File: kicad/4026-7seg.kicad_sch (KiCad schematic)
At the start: 2 parts, among them U5 D168K, U6 4026

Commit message: Note BOM effects in different implementations
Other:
- note added: "KNOWN ISSUES: * no easy reset * starts at 0, not 1 BOM ADDITION: 2"
- note removed: "KNOWN ISSUES: * no easy reset * starts at 0, not 1"
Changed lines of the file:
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@@
     (stroke (width 0) (type default) (color 0 0 0 0))
   )
-  (text "KNOWN ISSUES:\n* no easy reset\n* starts at 0, not 1"
-    (at 154.305 121.285 0)
+  (text "KNOWN ISSUES:\n* no easy reset\n* starts at 0, not 1\n\nBOM ADDITION: 2"
+    (at 153.67 127.635 0)
     (effects (font (size 1.27 1.27)) (justify left bottom))
   )

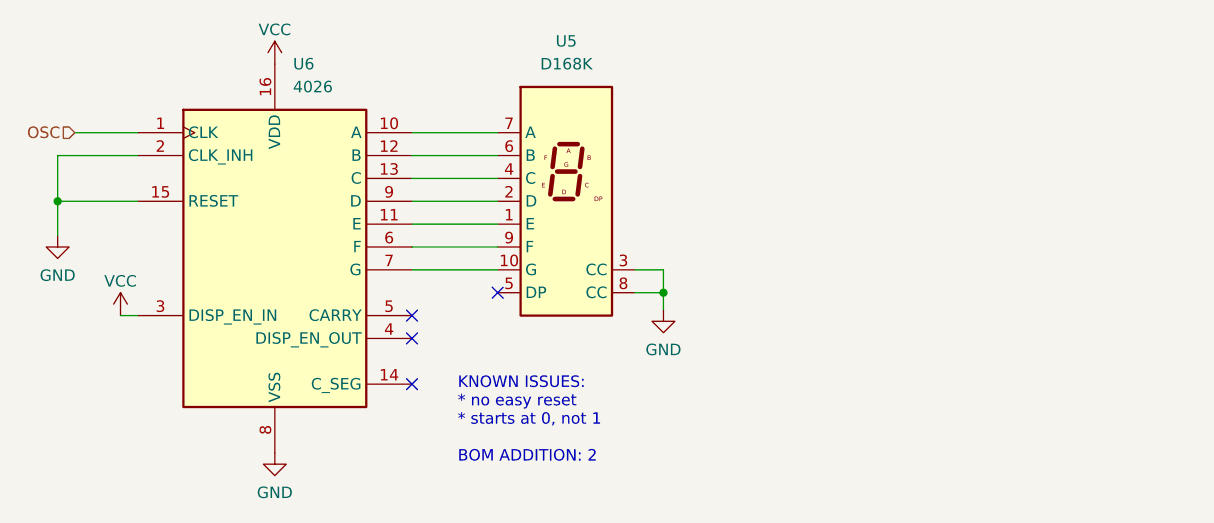
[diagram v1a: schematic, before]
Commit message: Hmmm, may need resistors for LED driver ICs
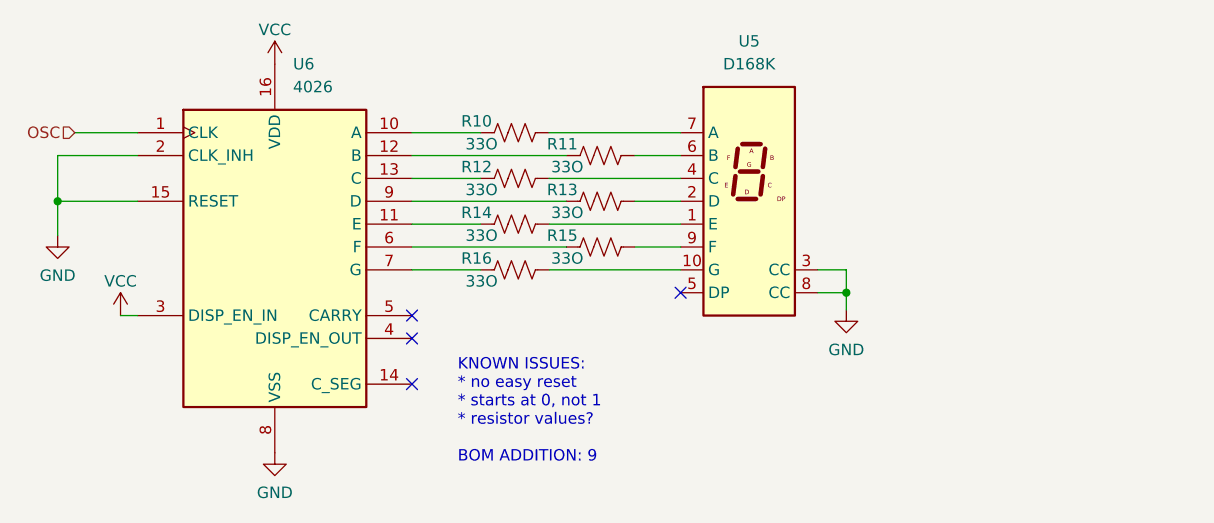
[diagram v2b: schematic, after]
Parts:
- added R10, R11, R12, R13, R14, R15, R16: 33O, Resistor_THT:R_Axial_DIN0204_L3.6mm_D1.6mm_P7.62mm_Horizontal, symbol Device:R_US
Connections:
- net at U5.1 (E): now also R14.2; no longer U6.11 (E)
- net at U5.10 (G): now also R16.2; no longer U6.7 (G)
- net at U5.2 (D): now also R13.2; no longer U6.9 (D)
- net at U6.13 (C): now also R12.1; no longer U5.4 (C)
- net at U5.6 (B): now also R11.2; no longer U6.12 (B)
- net at U5.7 (A): now also R10.2; no longer U6.10 (A)
- net at U6.6 (F): now also R15.1; no longer U5.9 (F)
- new net: R12.2, U5.4 (C)
- new net: R15.2, U5.9 (F)
- new net: R16.1, U6.7 (G)
- new net: R13.1, U6.9 (D)
- new net: R10.1, U6.10 (A)
- new net: R14.1, U6.11 (E)
- new net: R11.1, U6.12 (B)
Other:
- note added: "KNOWN ISSUES: * no easy reset * starts at 0, not 1 * resistor values? BOM ADDITION: 9"
- note removed: "KNOWN ISSUES: * no easy reset * starts at 0, not 1 BOM ADDITION: 2"
- moved on the sheet: U5

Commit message: TODO: fix 7seg footprint
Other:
- note added: "TODO: fix footprint! 10 A 9 B 7 C 5 D 4 E 2 F 1 G 6 DP 3 COM 8 COM"
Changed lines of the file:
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@@
+    (effects (font (size 1.27 1.27)) (justify left bottom))
+  )
+  (text "TODO: fix footprint!\n\n10 A\n9  B\n7  C\n5  D\n4  E\n2  F\n1  G\n\n6  DP\n3  COM\n8  COM"
+    (at 210.82 107.95 0)
     (effects (font (size 1.27 1.27)) (justify left bottom))
   )

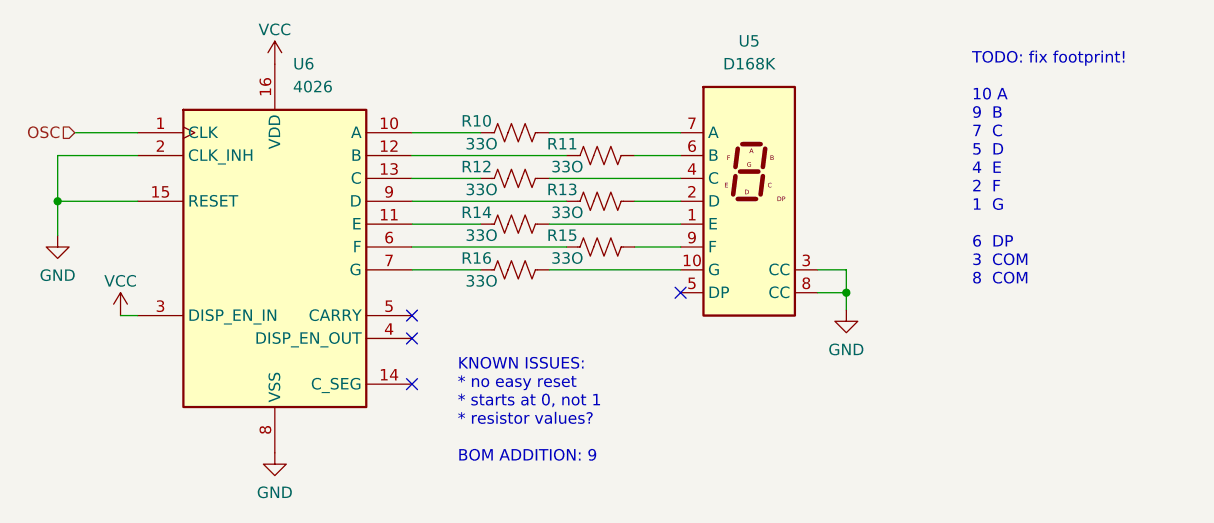
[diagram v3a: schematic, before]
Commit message: Fix 7seg footprint
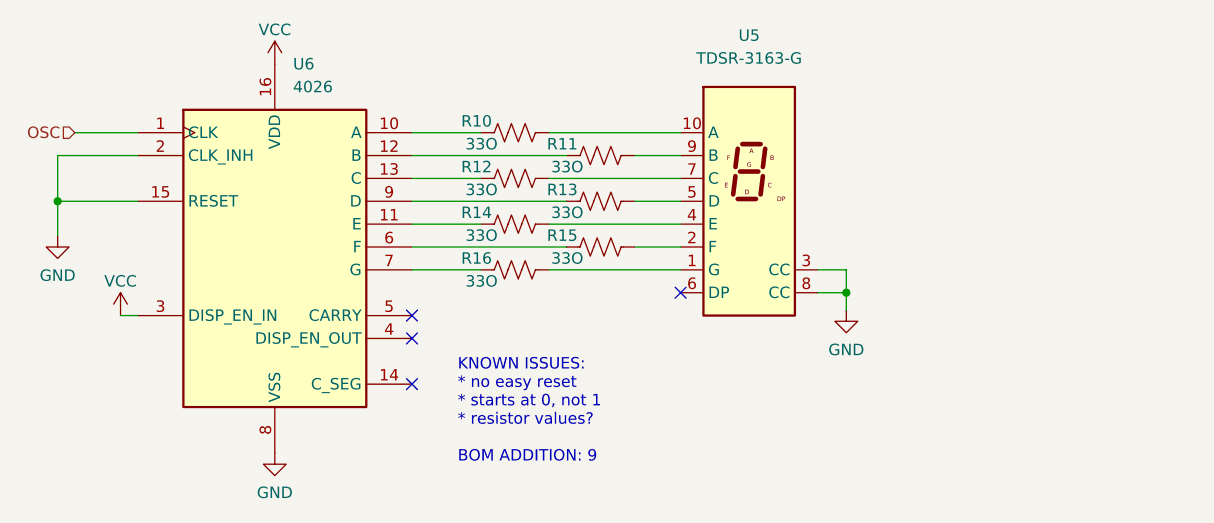
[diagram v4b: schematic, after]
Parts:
- removed U5: D168K, Display_7Segment:D1X8K, symbol Display_Character:D168K
- added U5: TDSR-3163-G, symbol parts_cafe:TDSR-3163-G
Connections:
- net GND: now also U5.3 (CC), U5.8 (CC)
- net at R12.2: now also U5.7 (C)
- net at R15.2: now also U5.2 (F)
- net at R14.2: now also U5.4 (E)
- net at R16.2: now also U5.1 (G)
- net at R13.2: now also U5.5 (D)
- net at R11.2: now also U5.9 (B)
- net at R10.2: now also U5.10 (A)
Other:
- note removed: "TODO: fix footprint! 10 A 9 B 7 C 5 D 4 E 2 F 1 G 6 DP 3 COM 8 COM"
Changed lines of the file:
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@@
-    (effects (font (size 1.27 1.27)) (justify left bottom))
-  )
-  (text "TODO: fix footprint!\n\n10 A\n9  B\n7  C\n5  D\n4  E\n2  F\n1  G\n\n6  DP\n3  COM\n8  COM"
-    (at 210.82 107.95 0)
     (effects (font (size 1.27 1.27)) (justify left bottom))
   )
@@
     )
     (pin "1")
+  )
+  (symbol (lib_id "parts_cafe:TDSR-3163-G") (at 180.975 84.455 0) (unit 1)
+    (in_bom yes) (on_board yes) (fields_autoplaced)
+    (property "Reference" "U5" (id 0) (at 186.055 80.01 0))
+    (property "Value" "TDSR-3163-G" (id 1) (at 186.055 82.55 0))
+    (property "Footprint" "" (id 2) (at 180.975 84.455 0)
+      (effects (font (size 1.27 1.27)) hide)
+    )
+    (property "Datasheet" "" (id 3) (at 180.975 84.455 0)
+      (effects (font (size 1.27 1.27)) hide)
+    )
+    (pin "1")
+    (pin "10")
+    (pin "2")
+    (pin "3")
+    (pin "4")
+    (pin "5")
+    (pin "6")
+    (pin "7")
+    (pin "8")
+    (pin "9")
   )
   (symbol (lib_id "Device:R_US") (at 160.02 95.885 90) (unit 1)
@@
     (pin "2")
   )
-  (symbol (lib_id "Display_Character:D168K") (at 186.055 98.425 0) (unit 1)
-    (in_bom yes) (on_board yes) (fields_autoplaced)
-    (property "Reference" "U5" (id 0) (at 186.055 80.645 0))
-    (property "Value" "D168K" (id 1) (at 186.055 83.185 0))
-    (property "Footprint" "Display_7Segment:D1X8K" (id 2) (at 186.055 113.665 0)
-      (effects (font (size 1.27 1.27)) hide)
-    )
-    (property "Datasheet" "https://ia800903.us.archive.org/24/items/CTKD1x8K/Cromatek%20D168K.pdf" (id 3) (at 173.355 86.36 0)
-      (effects (font (size 1.27 1.27)) (justify left) hide)
-    )
-    (pin "1")
-    (pin "10")
-    (pin "2")
-    (pin "3")
-    (pin "4")
-    (pin "5")
-    (pin "6")
-    (pin "7")
-    (pin "8")
-    (pin "9")
-  )
   (symbol (lib_id "power:GND") (at 196.85 110.49 0) (unit 1)

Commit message: Update to latest kicad
no functional changes
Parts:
- renumbered R12 to R11, R14 to R12, R16 to R13, R11 to R14, R13 to R15, R15 to R16, U6 to U5, U5 to U6
